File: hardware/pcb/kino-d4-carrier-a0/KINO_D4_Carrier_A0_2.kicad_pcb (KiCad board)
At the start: 4 copper layers, 117 x 69.4 mm, 250 parts, among them J100 P4 JP1 - 26 pin IDC, J1000 USB4105-GF-A, J101 C6 service - 3V3 sense only, J102 3V3 I2C accessory, J1100 PROTECTED 1S PACK / NTC, J1300 POWER PUSHBUTTON, J200 XIAO ESP32-S3 Sense socket, J201 GPIO breakout - SD/strap rest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, J300 XIAO ESP32-S3 Sense socket, J301 GPIO breakout - SD/strap rest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, J400 XIAO ESP32-S3 Sense socket, J401 GPIO breakout - SD/strap rest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, J500 XIAO ESP32-S3 Sense socket, J501 GPIO breakout - SD/strap rest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, J600 POGO TEST - SENSE ONLY, J601 EXTERNAL FLASH LOGIC, J800 3V PRIMARY RTC BACKUP, J900 HAPTIC MOTOR, J901 COVER HALL SENSOR, J902 LOCAL SHUTTER, J903 REMOTE DRY CONTACT, J904 FUNCTION BUTTON, Q1000 AO4407A, Q1001 AO4407A, Q1200 AO4407A, Q1201 AO4407A, Q1202 2N7002, Q1300 2N7002, Q900 2N7002, U100 TCA9517ADGKR, U1000 STUSB4500QTR, U1100 BQ25798RQMR, U1200 TPS61288LRQQR, U1201 TPS62162DSGR, U1300 LTC2955ITS8-1, U200 TXU0304PWR, U201 TPS2553DBVR, U300 TXU0304PWR, U301 TPS2553DBVR, U400 TXU0304PWR, U401 TPS2553DBVR, U500 TXU0304PWR, U501 TPS2553DBVR, U600 TCA9539PWR, U601 SN74LVC08APWR, U700 PAC1954T-E/4MX, U701 BQ27441DRZR-G1A, U800 LSM6DSOXTR, U801 RV-3028-C7, U802 TMP117AIDRVR, U900 DRV2605LDGSR, U901 SN74LVC1G14DBVR

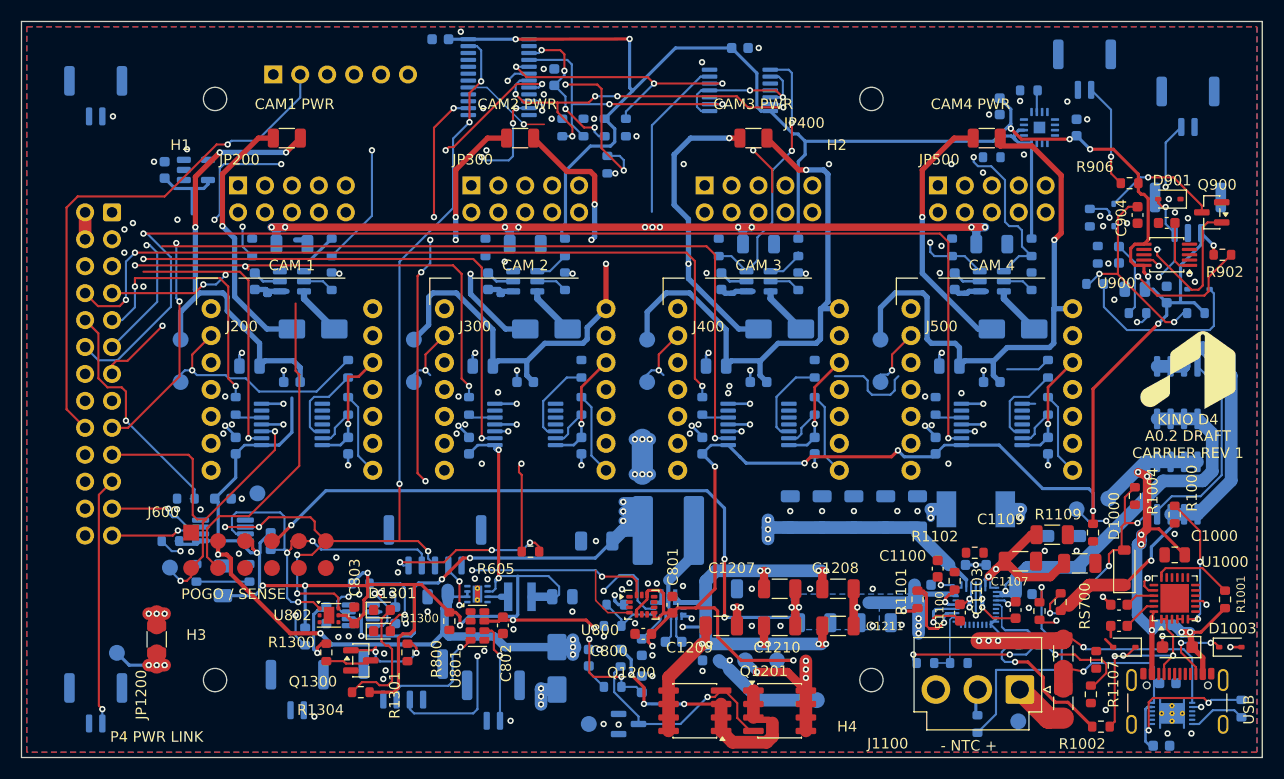
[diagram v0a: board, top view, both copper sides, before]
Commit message: feat(hardware): carrier A0.2 - second router pass, 101 -> 75 open
Re-routes the nets the camera GPIO template displaced plus a retry of
the rest; tidy pass; no clearance or short violations.

Co-Authored-By: Claude Opus 5.5 <noreply@anthropic.com>
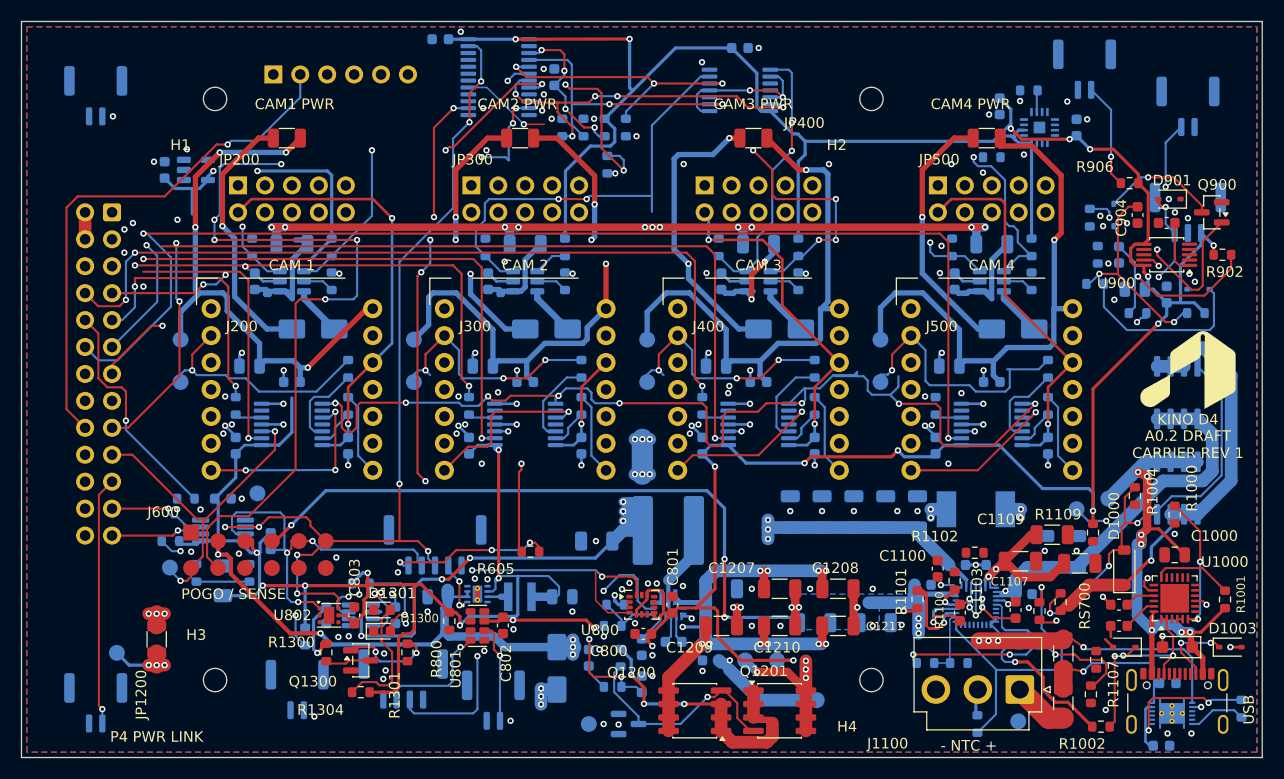
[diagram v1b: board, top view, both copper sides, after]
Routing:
- net P4_BUS_EN: track 14.8 -> 104.8 mm, vias 0 -> 8
- net CAM1_EN: track 88.3 -> 117.9 mm, vias 4 -> 7
- net CAM1_3V3: track 11.3 -> 40.9 mm, vias 1 -> 2
- net CAM2_EN: track 15.5 -> 40.4 mm, vias 0 -> 2
- net CAM4_3V3: track 10.8 -> 35.4 mm
- net CAM3_3V3: track 10.8 -> 33.2 mm, vias 1 -> 2
- net CAM1_TX: track 0.00 -> 18.7 mm, vias 0 -> 3
- net MB_3V3: track 417.3 -> 435.3 mm, vias 23 -> 25
- net CAM2_TX: track 0.00 -> 16.9 mm, vias 0 -> 1
- net CAM3_SYNC: track 6.61 -> 23.2 mm, vias 1 -> 3
- net CAM2_SYNC: track 6.61 -> 23.2 mm, vias 1 -> 3
- net CAM4_TX: track 0.00 -> 15.5 mm, vias 0 -> 1
- net CAM3_TX: track 0.00 -> 15.5 mm, vias 0 -> 1
- net CAM4_SYNC: track 10.2 -> 25.3 mm
- net CAM3_FAULT_N: track 39.9 -> 54.3 mm, vias 3 -> 6
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
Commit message: fix(hardware): carrier A0.2 - ground five GND pins that reached no ground
U900.4/.8 (haptic driver, front), U701.3 (gauge), C1101.2 (REGN cap)
and U1201.1 (buck PGND, tied to its exposed pad as in TI's layout) had
pour fragments with no via. New helpers gnd_pad_vias.py and rip_box.py;
CHG_REGN, REMOTE_ACTIVE and HAPTIC_REG re-routed clear of the new ground
copper. GND now has no open connection; 73 connections open in total.

Co-Authored-By: Claude Opus 5.5 <noreply@anthropic.com>
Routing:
- net CAM2_EN: track 40.4 -> 19.9 mm
- net REMOTE_ACTIVE: track 21.6 -> 32.3 mm, vias 2 -> 3
- net MB_3V3: track 435.3 -> 425.3 mm
- net GND: track 66.3 -> 76.0 mm, vias 146 -> 153
- net HAPTIC_REG: track 5.14 -> 12.5 mm, vias 0 -> 2
- net IMU_INT: track 15.1 -> 8.71 mm, vias 1 -> 0
- net CAM4_SYNC: track 25.3 -> 19.3 mm
- net CAM2_SYNC: track 23.2 -> 18.6 mm, vias 3 -> 2
- net CHG_REGN: track 38.7 -> 41.8 mm, vias 4 -> 6
- net P4_BUS_EN: track 104.8 -> 102.8 mm
- net CAM1_EN: track 117.9 -> 117.0 mm
- net CAM3_SYNC: track 23.2 -> 22.6 mm

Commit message: feat(hardware): carrier A0.2 - U700 to the camera row centre, Kelvin pairs from all four shunts
PAC1954 U700 moves to the front between the camera 2 and 3 headers. Eight
0.15 mm sense lines at 0.32 mm pitch run from the inner pad corners of
RS200-RS500 to it: cameras 2 and 3 along their header row gaps, cameras 1
and 4 through an In2 corridor north of the control lanes. Each sense line
touches only its shunt pad and its U700 pin (check_a02_kelvin.py). DRC has
no clearance or short errors; 79 connections open, re-routed next.

Co-Authored-By: Claude Opus 5.5 <noreply@anthropic.com>
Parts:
- C700, R700, U700: moved to F.Cu
- moved C700 42.6 mm to (107.7, 68.4), turned to 180 degrees
- moved U700 37.7 mm to (108.8, 65.5), turned to 90 degrees
- moved R700 36.1 mm to (110.9, 68.4), turned to 0 degrees
- moved C701 35.4 mm to (108.1, 67.2), turned to 0 degrees
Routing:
- net SYS_5V: track 237.7 -> 369.0 mm, vias 26 -> 32
- net MB_3V3: track 425.3 -> 341.5 mm, vias 25 -> 21
- net CAM4_SHUNT_OUT: track 10.4 -> 58.6 mm, vias 0 -> 2
- net CAM1_SHUNT_OUT: track 12.3 -> 53.9 mm, vias 0 -> 2
- net CAM4_REQ: track 34.6 -> 0.00 mm, vias 5 -> 0
- net CAM3_EN: track 25.8 -> 0.00 mm, vias 2 -> 0
- net CAM3_REQ: track 23.5 -> 0.81 mm, vias 3 -> 0
- net CAM2_EN: track 19.9 -> 3.20 mm, vias 2 -> 0
- net CAM3_SHUNT_OUT: track 10.2 -> 26.9 mm, vias 2 -> 3
- net CAM4_FAULT_N: track 71.3 -> 55.5 mm
- net CAM2_SHUNT_OUT: track 9.68 -> 23.7 mm, vias 0 -> 1
- net IMU_INT: track 8.71 -> 0.00 mm
- net CAM3_FAULT_N: track 54.3 -> 47.9 mm, vias 6 -> 5
- net GND: track 76.0 -> 81.3 mm, vias 153 -> 156
- net PAC_ADDR: track 2.22 -> 3.63 mm
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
